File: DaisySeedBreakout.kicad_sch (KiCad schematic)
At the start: 55 parts, among them J10 Conn_01x03, J11 Conn_01x03, J12 Conn_01x03, J13 Conn_01x03, J14 Conn_01x03, J15 Conn_02x08, J2 Conn_02x08, J36 MJ-3523-SMT-TR, J37 MJ-3523-SMT-TR, J38 MJ-3523-SMT-TR, J39 MJ-3523-SMT-TR, J40 MJ-3523-SMT-TR, J41 MJ-3523-SMT-TR, J42 MJ-3523-SMT-TR, J43 MJ-3523-SMT-TR, J44 MJ-3523-SMT-TR, J45 MJ-3523-SMT-TR, J5 Conn_02x08, J6 Conn_01x03, J8 Conn_01x03, J9 Conn_01x03, U2 H11L1M

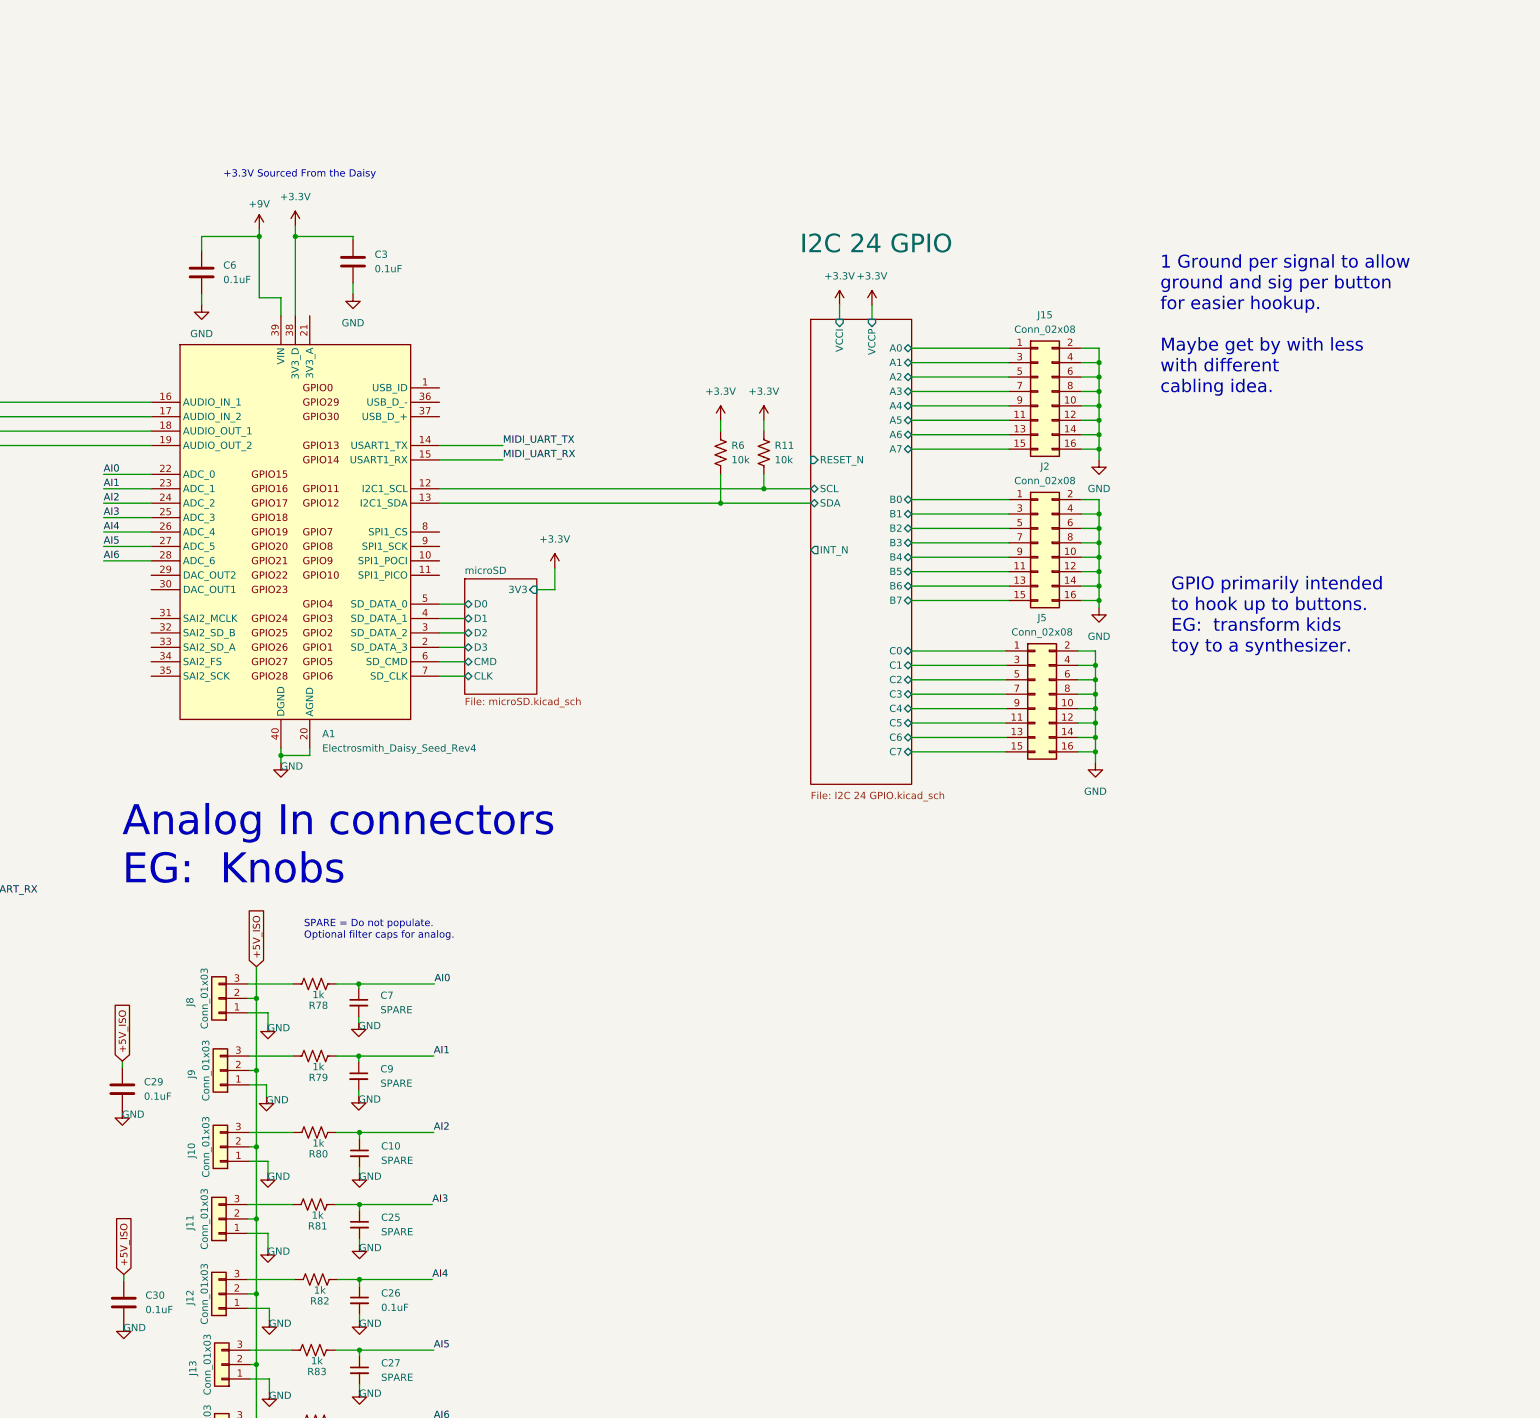
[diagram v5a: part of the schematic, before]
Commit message: update design to use more headers.  Need to figure out easy way to integrate connectors in modular but easy to use way without dangling wires
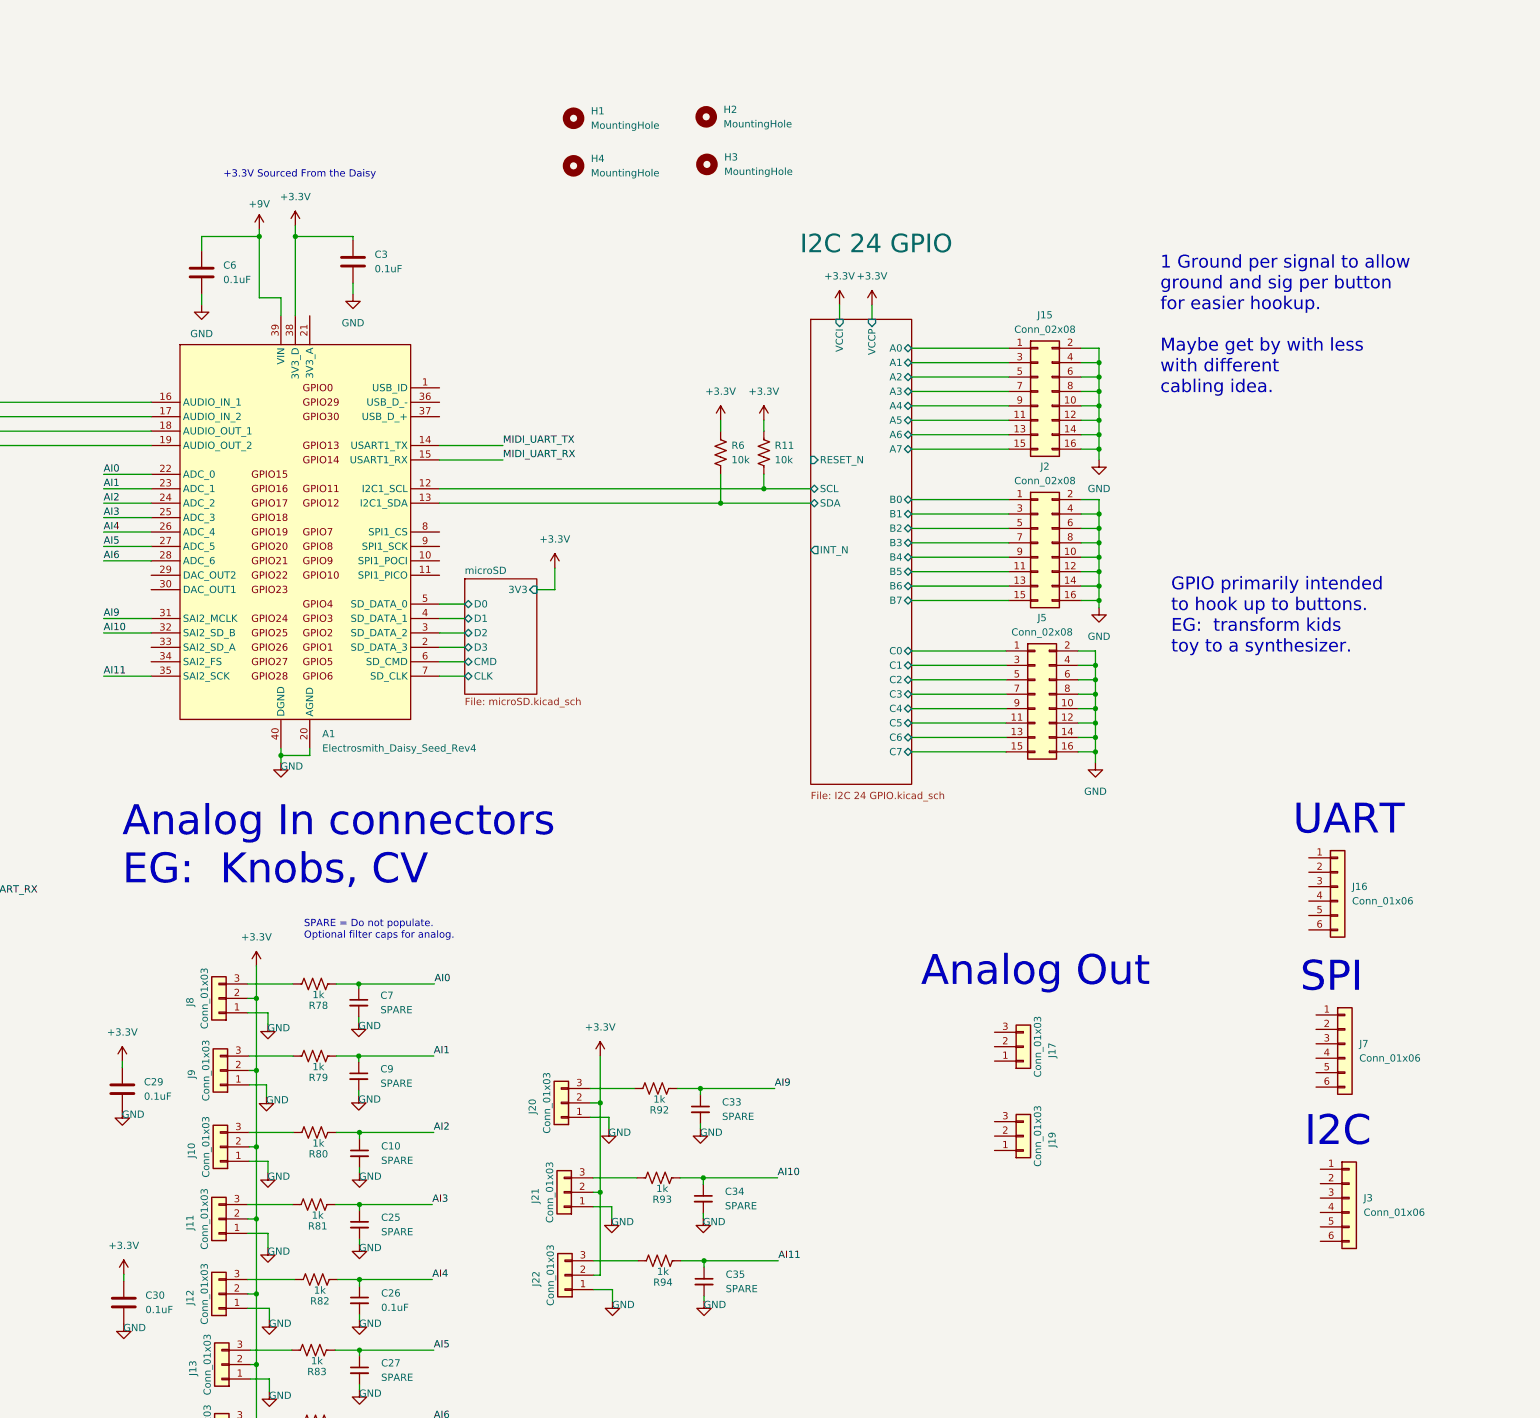
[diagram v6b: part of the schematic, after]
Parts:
- added C33, C34, C35: SPARE, Capacitor_SMD:C_0402_1005Metric, symbol Device:C_Small
- added H1, H2, H3, H4: MountingHole, MountingHole:MountingHole_3.2mm_M3_DIN965_Pad, symbol Mechanical:MountingHole
- added J16, J3: Conn_01x06, Ultralibrarian:PinHeader_1x06_P2.54mm_Vertical_Female, symbol 4ms_Connector:Conn_01x06
- added J17, J19, J20, J21, J22: Conn_01x03, Ultralibrarian:PinHeader_1x03_P2.54mm_Vertical_Female, symbol 4ms_Connector:Conn_01x03
- added J7: Conn_01x06, Ultralibrarian:PinHeader_2x08_P2.54mm_Vertical_Female, symbol 4ms_Connector:Conn_01x06
- added R92, R93, R94: 1k, Resistor_SMD:R_0402_1005Metric, symbol Device:R_US
- J10, J11, J12, J13, J14, J8, J9: footprint Connector_PinHeader_2.54mm:PinHeader_1x03_P2.54mm_Vertical -> Ultralibrarian:PinHeader_1x03_P2.54mm_Vertical_Female
- J15: footprint Connector_PinHeader_2.54mm:PinHeader_2x08_P2.54mm_Vertical -> Ultralibrarian:PinHeader_2x08_P2.54mm_Vertical_Female
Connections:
- net +3.3V: now also C29.1, C30.1, J10.2 (Pin_2), J11.2 (Pin_2), J12.2 (Pin_2), J13.2 (Pin_2), J14.2 (Pin_2), J8.2 (Pin_2), J9.2 (Pin_2), J20.2 (Pin_2), J21.2 (Pin_2), J22.2 (Pin_2)
- net +5V_ISO: no longer C29.1, C30.1, J10.2 (Pin_2), J11.2 (Pin_2), J12.2 (Pin_2), J13.2 (Pin_2), J14.2 (Pin_2), J8.2 (Pin_2), J9.2 (Pin_2)
- net GND: now also C33.2, C34.2, C35.2, J20.1 (Pin_1), J21.1 (Pin_1), J22.1 (Pin_1)
- net AI9: now reaches A1.31 (SAI2_MCLK)
- net AI9: now also C33.1, R92.1
- net AI10: now reaches A1.32 (SAI2_SD_B)
- net AI10: now also C34.1, R93.1
- net AI11: now reaches A1.35 (SAI2_SCK)
- net AI11: now also C35.1, R94.1
- new net: J20.3 (Pin_3), R92.2
- new net: J22.3 (Pin_3), R94.2
- new net: J21.3 (Pin_3), R93.2
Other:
- note added: "Analog In connectors EG: Knobs, CV"
- note added: "Analog Out"
- note added: "I2C"
- note added: "SPI"
- note added: "UART"
- note removed: "Analog In connectors EG: Knobs"

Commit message: added dual audio back in to prototype that concept
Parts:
- removed C31: 0.1uF, Capacitor_SMD:C_0603_1608Metric, symbol Device:C_Small
- removed J16, J3: Conn_01x06, Ultralibrarian:PinHeader_1x06_P2.54mm_Vertical_Female, symbol 4ms_Connector:Conn_01x06
- removed J6: Conn_01x03, Connector_PinHeader_2.54mm:PinHeader_1x03_P2.54mm_Vertical, symbol 4ms_Connector:Conn_01x03
- removed J7: Conn_01x06, Ultralibrarian:PinHeader_2x08_P2.54mm_Vertical_Female, symbol 4ms_Connector:Conn_01x06
- added J16, J23, J28, J29, J3, J7: Conn_01x03, Ultralibrarian:PinHeader_1x03_P2.54mm_Vertical_Female, symbol 4ms_Connector:Conn_01x03
- added J24, J25, J30, J32, J33, J34, J35, J46, J6: Conn_01x02, Connector_PinHeader_2.54mm:PinHeader_1x02_P2.54mm_Vertical, symbol 4ms_Connector:Conn_01x02
- added J26, J31: Conn_02x04, Connector_PinHeader_2.54mm:PinHeader_2x04_P2.54mm_Vertical, symbol 4ms_Connector:Conn_02x04
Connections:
- net Audio In Sum/AUDIO_IN_L_CONN: now also J24.1 (Pin_1)
- net Audio In Sum/AUDIO_IN_R_CONN: now also J25.1 (Pin_1)
- net Audio Out/AUDIO_OUT_L_EXT: now also J6.1 (Pin_1)
- net Audio Out/AUDIO_OUT_R_EXT: now also J30.1 (Pin_1)
- net GND: now also J24.2 (Pin_2), J25.2 (Pin_2), J28.3 (Pin_3), J29.3 (Pin_3), J30.2 (Pin_2), J6.2 (Pin_2)
- net at J1.2B, R87.2, R88.2: now also J28.2 (Pin_2)
- net at J1.2A, R90.2: now also J29.2 (Pin_2)
- net at J1.5A, R91.2: now also J29.1 (Pin_1)
- net at J1.5B, R85.2, R86.2: now also J28.1 (Pin_1)
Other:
- note added: "3.3V"
- note added: "5V"
- note added: "USB 2.0"
- note added: "VIN"
- note added: "VOUT"
- moved on the sheet: R90, R91

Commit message: Converted circuits to sub circuits.  Removed MIDI connector, changed to header only
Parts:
- removed C10, C25, C27, C28, C33, C34, C35, C7, C9: SPARE, Capacitor_SMD:C_0402_1005Metric, symbol Device:C_Small
- removed C26: 0.1uF, Capacitor_SMD:C_0402_1005Metric, symbol Device:C_Small
- removed C29, C30: 0.1uF, Capacitor_SMD:C_0402_1005Metric, symbol Device:C
- removed C32: 0.1uF, Capacitor_SMD:C_0603_1608Metric, symbol Device:C_Small
- removed D1: D_Schottky, Diode_SMD:D_0402_1005Metric, symbol Device:D_Schottky_Small
- removed J1: ~, Ultralibrarian:STX-4235-3-3-N, symbol Ultralibrarian_modified_symbols:STX-4235-3-3-N
- removed J10, J11, J12, J13, J14, J16, J17, J19, J20, J21, J22, J23, J28, J29, J3, J7, J8, J9: Conn_01x03, Ultralibrarian:PinHeader_1x03_P2.54mm_Vertical_Female, symbol 4ms_Connector:Conn_01x03
- removed J15: Conn_02x08, Ultralibrarian:PinHeader_2x08_P2.54mm_Vertical_Female, symbol 4ms_Connector:Conn_02x08
- removed J2, J5: Conn_02x08, Connector_PinHeader_2.54mm:PinHeader_2x08_P2.54mm_Vertical, symbol 4ms_Connector:Conn_02x08
- removed J36, J37, J38, J39, J40, J41, J42, J43, J44, J45: MJ-3523-SMT-TR, SurfaceMountAudiofootprints:MJ-3523-SMT-TR, symbol 2023-09-25_23-43-35:MJ-3523-SMT-TR
- removed J46: Conn_01x02, Connector_PinHeader_2.54mm:PinHeader_1x02_P2.54mm_Vertical, symbol 4ms_Connector:Conn_01x02
- removed R78, R79, R80, R81, R82, R83, R84, R92, R93, R94: 1k, Resistor_SMD:R_0402_1005Metric, symbol Device:R_US
- removed R85: 220, Resistor_SMD:R_0402_1005Metric, symbol Device:R_US
- removed R86, R87: SPARE, Resistor_SMD:R_0402_1005Metric, symbol Device:R_US
- removed R88: 0, Resistor_SMD:R_0402_1005Metric, symbol Device:R_US
- removed R89: 270, Resistor_SMD:R_0402_1005Metric, symbol Device:R_US
- removed R90: 10, Resistor_SMD:R_0402_1005Metric, symbol Device:R_US
- removed R91: 33, Resistor_SMD:R_0402_1005Metric, symbol Device:R_US
- removed U2: H11L1M, digikey-footprints:DIP-6_W7.62mm, symbol dk_Optoisolators-Logic-Output:H11L1M
- added R48, R49, R50, R51: 10k, Resistor_SMD:R_0402_1005Metric, symbol Device:R_US
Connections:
- net +3.3V: now also R48.1, R49.1, R50.1, R51.1
- net arduino_coprocessor/UART0_RXD_SPI0_MISO: now reaches A1.10 (SPI1_POCI)
- net arduino_coprocessor/UART0_TXD_SPI0_MOSI: now reaches A1.11 (SPI1_PICO)
- net Analog_out_conn/AO_Conn: now reaches A1.29 (DAC_OUT2)
- net Analog_out_conn1/AO_Conn: now reaches A1.30 (DAC_OUT1)
- net RESET_n: now reaches A1.33 (SAI2_SD_A)
- net UPDI: now reaches A1.34 (SAI2_FS)
- net arduino_coprocessor/SPI0_CS: now reaches A1.8 (SPI1_CS)
- net arduino_coprocessor/SPI0_SCLK: now reaches A1.9 (SPI1_SCK)
- net I2C 24 GPIO/SCL renamed GPIO_Conn11/GPIO_Conn
- net I2C 24 GPIO/SDA renamed GPIO_Conn12/GPIO_Conn
- new net GPIO_Conn/GPIO_Conn: R51.2
- new net GPIO_Conn1/GPIO_Conn: R50.2
- new net GPIO_Conn2/GPIO_Conn: R49.2
- new net GPIO_Conn3/GPIO_Conn: R48.2
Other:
- removed sheet I2C 24 GPIO
- added sheet AI_GPIO (AI_GPIO.kicad_sch)
- added sheet AI_GPIO1 (AI_GPIO.kicad_sch)
- added sheet AI_GPIO10 (AI_GPIO.kicad_sch)
- added sheet AI_GPIO11 (AI_GPIO.kicad_sch)
- added sheet AI_GPIO12 (AI_GPIO.kicad_sch)
- added sheet AI_GPIO13 (AI_GPIO.kicad_sch)
- added sheet AI_GPIO14 (AI_GPIO.kicad_sch)
- added sheet AI_GPIO15 (AI_GPIO.kicad_sch)
- added sheet AI_GPIO16 (AI_GPIO.kicad_sch)
- added sheet AI_GPIO17 (AI_GPIO.kicad_sch)
- added sheet AI_GPIO18 (AI_GPIO.kicad_sch)
- added sheet AI_GPIO19 (AI_GPIO.kicad_sch)
- added sheet AI_GPIO2 (AI_GPIO.kicad_sch)
- added sheet AI_GPIO3 (AI_GPIO.kicad_sch)
- added sheet AI_GPIO4 (AI_GPIO.kicad_sch)
- added sheet AI_GPIO5 (AI_GPIO.kicad_sch)
- added sheet AI_GPIO6 (AI_GPIO.kicad_sch)
- added sheet AI_GPIO7 (AI_GPIO.kicad_sch)
- added sheet AI_GPIO8 (AI_GPIO.kicad_sch)
- added sheet AI_GPIO9 (AI_GPIO.kicad_sch)
- added sheet Analog_out_conn (Analog_out_conn.kicad_sch)
- added sheet Analog_out_conn1 (Analog_out_conn.kicad_sch)
- added sheet GPIO_Conn (GPIO_Conn.kicad_sch)
- added sheet GPIO_Conn1 (GPIO_Conn.kicad_sch)
- added sheet GPIO_Conn10 (GPIO_Conn.kicad_sch)
- added sheet GPIO_Conn11 (GPIO_Conn.kicad_sch)
- added sheet GPIO_Conn12 (GPIO_Conn.kicad_sch)
- added sheet GPIO_Conn2 (GPIO_Conn.kicad_sch)
- added sheet GPIO_Conn3 (GPIO_Conn.kicad_sch)
- added sheet GPIO_Conn4 (GPIO_Conn.kicad_sch)
- added sheet GPIO_Conn5 (GPIO_Conn.kicad_sch)
- added sheet GPIO_Conn6 (GPIO_Conn.kicad_sch)
- added sheet GPIO_Conn7 (GPIO_Conn.kicad_sch)
- added sheet GPIO_Conn8 (GPIO_Conn.kicad_sch)
- added sheet GPIO_Conn9 (GPIO_Conn.kicad_sch)
- added sheet MIDI_IN (MIDI_IN.kicad_sch)
- added sheet MIDI_OUT (MIDI_OUT.kicad_sch)
- added sheet arduino_coprocessor (arduino_coprocessor.kicad_sch)
- note added: "Accelerometer/Magnometer/Gyroscope/Temperature Sensor"
- note added: "Power/Battery connector/Input protection"
- note added: "Speaker Driver"
- note added: "Sprinkle Decoupling Bulk Decoupling"
- note removed: "1 Ground per signal to allow ground and sig per button for easier hookup. Maybe get by with less with different cabling idea."
- note removed: "Accelerometer/Magnometer/Temperature Sensor"
- note removed: "Analog Out"
- note removed: "GPIO primarily intended to hook up to buttons. EG: transform kids toy to a synthesizer."
- note removed: "I2C"
- note removed: "MIDI IN"
- note removed: "MIDI OUT"
- note removed: "Power/Battery connector"
- note removed: "SPARE = Do not populate. Optional filter caps for analog."
- note removed: "SPI"
- note removed: "UART"
- moved on the sheet: J26, J31, J32, J33, J34, J35, R11, R6
